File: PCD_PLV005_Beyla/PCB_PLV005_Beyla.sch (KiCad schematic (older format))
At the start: 5 parts, among them J1 PWR/QB, J2 Switch_In, U7 CRE1S2405SC

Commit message: Add Heartbeat_Buff signal pin
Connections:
- wire segments 31 -> 30
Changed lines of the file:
@@
 EESchema Schematic File Version 4
-EELAYER 30 0
+LIBS:PCB_PLV005_Beyla-cache
+EELAYER 29 0
 EELAYER END
 $Descr USLetter 11000 8500
@@
 F6 "HEARTBEAT_ADDRESS_4" O R 6000 4450 50
 F7 "HEARTBEAT" O R 6000 4600 50
+F8 "HEARTBEAT_BUFF" O R 6000 4700 50
 $EndSheet
 $Comp
@@
 $EndComp
 Wire Wire Line
-	4850 3000 4650 3000
-Connection ~ 4650 3000
-Wire Wire Line
 	4650 3000 4250 3000

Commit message: Beyla Schematic Changes
Addressed changes from review of initial schematic
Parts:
- removed D1: Red, symbol PCB_PLV005_Beyla-rescue:TemplateProject-rescue_LED-Device-TemplateProject-cache
- removed J1: PWR/QB, symbol Connector:Conn_01x08_Female
- removed J2: Switch_In, symbol Connector:Conn_01x04_Female
- removed R18: 1k, symbol TemplateProject-rescue:R_US-Device
- removed U7: CRE1S2405SC, Converter_DCDC:Converter_DCDC_muRata_CRE1xxxxxxSC_THT, symbol Regulator_Switching:CRE1S2405SC
- added C8: 1uF, symbol Device:C
- added C9: 10uF, symbol Device:C
- added D1: RED, symbol Device:LED
- added J1: PWR/QB, symbol Connector_Generic:Conn_01x08
- added J2: Switch_In, symbol Connector_Generic:Conn_01x04
- added R18: 1k, symbol Device:R_US
- added R19: 0, symbol Device:R_US
- added VR1: Recom_R-78c-1.0, symbol boringlib:Recom_R-78c-1.0
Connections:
- net labels added: +5V
- wire segments 30 -> 41
- no-connect marks 0 -> 1
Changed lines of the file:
@@
 EESchema Schematic File Version 4
-LIBS:PCB_PLV005_Beyla-cache
-EELAYER 29 0
+EELAYER 30 0
 EELAYER END
 $Descr USLetter 11000 8500
@@
 	1    0    0    -1
 $EndComp
-$Comp
-L Connector:Conn_01x08_Female J1
-U 1 1 5FB80BE7
+Wire Wire Line
+	7100 3950 6900 3950
+Wire Wire Line
+	6900 3350 7100 3350
+Wire Wire Line
+	7100 3350 7100 3450
+Wire Wire Line
+	6250 4600 6000 4600
+Wire Wire Line
+	6250 4550 7100 4550
+Wire Wire Line
+	6000 4450 7100 4450
+Wire Wire Line
+	6000 4350 7100 4350
+Wire Wire Line
+	6000 4250 7100 4250
+Wire Wire Line
+	6000 4150 7100 4150
+Wire Wire Line
+	6250 4550 6250 4600
+Wire Wire Line
+	4100 4150 2800 4150
+Wire Wire Line
+	2650 4250 2800 4250
+Wire Wire Line
+	2800 4250 2800 4150
+Connection ~ 2800 4150
+Wire Wire Line
+	2800 4150 2650 4150
+Wire Wire Line
+	2650 4450 2800 4450
+$Comp
+L power:GND #PWR0102
+U 1 1 5FB9ACDA
+P 2800 5100
+F 0 "#PWR0102" H 2800 4850 50  0001 C CNN
+F 1 "GND" H 2805 4927 50  0000 C CNN
+F 2 "" H 2800 5100 50  0001 C CNN
+F 3 "" H 2800 5100 50  0001 C CNN
+	1    2800 5100
+	1    0    0    -1
+$EndComp
+Wire Wire Line
+	6900 3350 6900 3600
+Wire Wire Line
+	7100 4050 6250 4050
+Wire Wire Line
+	6250 4050 6250 3000
+Wire Wire Line
+	6250 3000 5800 3000
+$Comp
+L Device:C C8
+U 1 1 5FBF38DA
+P 5800 3300
+F 0 "C8" H 5915 3346 50  0000 L CNN
+F 1 "1uF" H 5915 3255 50  0000 L CNN
+F 2 "" H 5838 3150 50  0001 C CNN
+F 3 "~" H 5800 3300 50  0001 C CNN
+	1    5800 3300
+	1    0    0    -1
+$EndComp
+$Comp
+L Device:C C9
+U 1 1 5FBF4C36
+P 4550 3300
+F 0 "C9" H 4665 3346 50  0000 L CNN
+F 1 "10uF" H 4665 3255 50  0000 L CNN
+F 2 "" H 4588 3150 50  0001 C CNN
+F 3 "~" H 4550 3300 50  0001 C CNN
+	1    4550 3300
+	1    0    0    -1
+$EndComp
+Wire Wire Line
+	6900 3600 5800 3600
+Connection ~ 6900 3600
+Wire Wire Line
+	6900 3600 6900 3950
+Wire Wire Line
+	5200 3600 5200 3350
+Wire Wire Line
+	5800 3450 5800 3600
+Connection ~ 5800 3600
+Wire Wire Line
+	5800 3600 5200 3600
+Wire Wire Line
+	5800 3150 5800 3000
+Connection ~ 5800 3000
+Wire Wire Line
+	5800 3000 5600 3000
+Wire Wire Line
+	4800 3000 4550 3000
+Wire Wire Line
+	4550 3000 4550 3150
+Wire Wire Line
+	4550 3450 4550 3600
+Wire Wire Line
+	4550 3600 5200 3600
+Connection ~ 5200 3600
+$Comp
+L power:+5V #PWR0103
+U 1 1 5FBFDEDC
+P 4550 2950
+F 0 "#PWR0103" H 4550 2800 50  0001 C CNN
+F 1 "+5V" H 4565 3123 50  0000 C CNN
+F 2 "" H 4550 2950 50  0001 C CNN
+F 3 "" H 4550 2950 50  0001 C CNN
+	1    4550 2950
+	1    0    0    -1
+$EndComp
+Connection ~ 4550 3000
+$Comp
+L Device:LED D1
+U 1 1 5FBFEF04
+P 4050 3000
+F 0 "D1" H 4043 3217 50  0000 C CNN
+F 1 "RED" H 4043 3126 50  0000 C CNN
+F 2 "" H 4050 3000 50  0001 C CNN
+F 3 "~" H 4050 3000 50  0001 C CNN
+	1    4050 3000
+	1    0    0    -1
+$EndComp
+$Comp
+L Device:R_US R18
+U 1 1 5FC06267
+P 3550 3300
+F 0 "R18" H 3618 3346 50  0000 L CNN
+F 1 "1k" H 3618 3255 50  0000 L CNN
+F 2 "" V 3590 3290 50  0001 C CNN
+F 3 "~" H 3550 3300 50  0001 C CNN
+	1    3550 3300
+	1    0    0    -1
+$EndComp
+Wire Wire Line
+	3900 3000 3550 3000
+Wire Wire Line
+	3550 3000 3550 3150
+Wire Wire Line
+	3550 3450 3550 3600
+Wire Wire Line
+	3550 3600 4550 3600
+Connection ~ 4550 3600
+Wire Wire Line
+	4200 3000 4550 3000
+$Comp
+L boringlib:Recom_R-78c-1.0 VR1
+U 1 1 5FC17AF0
+P 5200 3000
+F 0 "VR1" H 5200 3315 50  0000 C CNN
+F 1 "Recom_R-78c-1.0" H 5200 3224 50  0000 C CNN
+F 2 "" H 5400 2700 50  0001 C CNN
+F 3 "https://d311uvhi8lkjbj.cloudfront.net/media/Datasheet/pdf/.f91HWzyW/.t321978fcd1ad139cbfa2/Datasheet-260/R-78C-1_0.pdf" H 5400 2700 50  0001 C CNN
+	1    5200 3000
+	-1   0    0    -1
+$EndComp
+NoConn ~ 7100 4650
+Wire Wire Line
+	4550 2950 4550 3000
+$Comp
+L Connector_Generic:Conn_01x08 J1
+U 1 1 5FC2996A
 P 7300 4250
-F 0 "J1" H 7328 4226 50  0000 L CNN
-F 1 "PWR/QB" H 7328 4135 50  0000 L CNN
+F 0 "J1" H 7380 4242 50  0000 L CNN
+F 1 "PWR/QB" H 7380 4151 50  0000 L CNN
 F 2 "" H 7300 4250 50  0001 C CNN
 F 3 "~" H 7300 4250 50  0001 C CNN
@@
 	1    0    0    -1
 $EndComp
-Wire Wire Line
-	7100 3950 6900 3950
-Wire Wire Line
-	6900 3950 6900 3400
-Wire Wire Line
-	6900 3350 7100 3350
-Wire Wire Line
-	7100 3350 7100 3450
-Wire Wire Line
-	6250 4600 6000 4600
-Wire Wire Line
-	6250 4550 7100 4550
-Wire Wire Line
-	6000 4450 7100 4450
-Wire Wire Line
-	6000 4350 7100 4350
-Wire Wire Line
-	6000 4250 7100 4250
-Wire Wire Line
-	6000 4150 7100 4150
-Wire Wire Line
-	6250 4550 6250 4600
-$Comp
-L Connector:Conn_01x04_Female J2
-U 1 1 5FB96598
+$Comp
+L Connector_Generic:Conn_01x04 J2
+U 1 1 5FC2E912
 P 2450 4350
-F 0 "J2" H 2342 3925 50  0000 C CNN
-F 1 "Switch_In" H 2342 4016 50  0000 C CNN
+F 0 "J2" H 2368 3925 50  0000 C CNN
+F 1 "Switch_In" H 2368 4016 50  0000 C CNN
 F 2 "" H 2450 4350 50  0001 C CNN
 F 3 "~" H 2450 4350 50  0001 C CNN
@@
 	-1   0    0    1
 $EndComp
-Wire Wire Line
-	4100 4150 2800 4150
-Wire Wire Line
-	2650 4250 2800 4250
-Wire Wire Line
-	2800 4250 2800 4150
-Connection ~ 2800 4150
-Wire Wire Line
-	2800 4150 2650 4150
-Wire Wire Line
-	2650 4450 2800 4450
-Wire Wire Line
-	2800 4350 2650 4350
+$Comp
+L Device:R_US R19
+U 1 1 5FC33E92
+P 2800 4850
+F 0 "R19" H 2868 4896 50  0000 L CNN
+F 1 "0" H 2868 4805 50  0000 L CNN
+F 2 "" V 2840 4840 50  0001 C CNN
+F 3 "~" H 2800 4850 50  0001 C CNN
+	1    2800 4850
+	1    0    0    -1
+$EndComp
+Wire Wire Line
+	2800 4450 2800 4700
+Wire Wire Line
+	2800 5100 2800 5000
+$Comp
+L power:+5V #PWR0104
+U 1 1 5FC3DBBE
+P 2900 4350
+F 0 "#PWR0104" H 2900 4200 50  0001 C CNN
+F 1 "+5V" H 2915 4523 50  0000 C CNN
+F 2 "" H 2900 4350 50  0001 C CNN
+F 3 "" H 2900 4350 50  0001 C CNN
+	1    2900 4350
+	1    0    0    -1
+$EndComp
+Wire Wire Line
+	2650 4350 2800 4350
 Wire Wire Line
 	2800 4350 2800 4450
 Connection ~ 2800 4450
 Wire Wire Line
-	2800 4450 2800 4600
-$Comp
-L power:GND #PWR0102
-U 1 1 5FB9ACDA
-P 2800 4600
-F 0 "#PWR0102" H 2800 4350 50  0001 C CNN
-F 1 "GND" H 2805 4427 50  0000 C CNN
-F 2 "" H 2800 4600 50  0001 C CNN
-F 3 "" H 2800 4600 50  0001 C CNN
-	1    2800 4600
-	1    0    0    -1
-$EndComp
-$Comp
-L Regulator_Switching:CRE1S2405SC U7
-U 1 1 5FB97432
-P 5150 3200
-F 0 "U7" H 5150 3667 50  0000 C CNN
-F 1 "CRE1S2405SC" H 5150 3576 50  0000 C CNN
-F 2 "Converter_DCDC:Converter_DCDC_muRata_CRE1xxxxxxSC_THT" H 5150 2800 50  0001 C CNN
-F 3 "http://power.murata.com/datasheet?/data/power/ncl/kdc_cre1.pdf" H 5150 2700 50  0001 C CNN
-	1    5150 3200
-	-1   0    0    -1
-$EndComp
-Wire Wire Line
-	6300 3000 5650 3000
-$Comp
-L PCB_PLV005_Beyla-rescue:TemplateProject-rescue_LED-Device-TemplateProject-cache D1
-U 1 1 5FBAAA01
-P 4100 3000
-F 0 "D1" H 4093 3216 50  0000 C CNN
-F 1 "Red" H 4093 3125 50  0000 C CNN
-F 2 "" H 4100 3000 50  0001 C CNN
-F 3 "" H 4100 3000 50  0001 C CNN
-	1    4100 3000
-	1    0    0    -1
-$EndComp
-$Comp
-L TemplateProject-rescue:R_US-Device R18
-U 1 1 5FBACDDB
-P 3650 3000
-F 0 "R18" V 3855 3000 50  0000 C CNN
-F 1 "1k" V 3764 3000 50  0000 C CNN
-F 2 "" V 3690 2990 50  0001 C CNN
-F 3 "" H 3650 3000 50  0001 C CNN
-	1    3650 3000
-	0    -1   -1   0
-$EndComp
-$Comp
-L power:GND #PWR0103
-U 1 1 5FBB007E
-P 3350 3000
-F 0 "#PWR0103" H 3350 2750 50  0001 C CNN
-F 1 "GND" H 3355 2827 50  0000 C CNN
-F 2 "" H 3350 3000 50  0001 C CNN
-F 3 "" H 3350 3000 50  0001 C CNN
-	1    3350 3000
-	0    1    1    0
-$EndComp
-Wire Wire Line
-	4650 3000 4250 3000
-Wire Wire Line
-	3950 3000 3800 3000
-Wire Wire Line
-	4650 3400 3400 3400
-Wire Wire Line
-	3350 3000 3400 3000
-Wire Wire Line
-	5650 3400 6900 3400
-Connection ~ 6900 3400
-Wire Wire Line
-	6900 3400 6900 3350
-Wire Wire Line
-	7100 4050 6300 4050
-Wire Wire Line
-	6300 4050 6300 3000
-Wire Wire Line
-	3400 3400 3400 3000
-Connection ~ 3400 3000
-Wire Wire Line
-	3400 3000 3500 3000
+	2900 4350 2800 4350
+Connection ~ 2800 4350
 $EndSCHEMATC

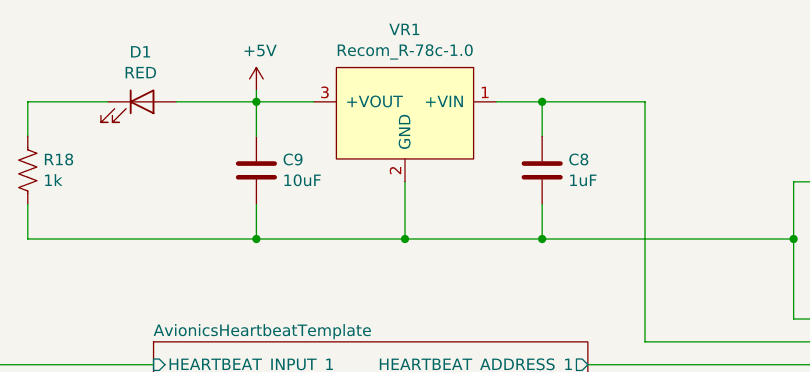
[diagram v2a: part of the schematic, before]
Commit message: Fix regulator issue.
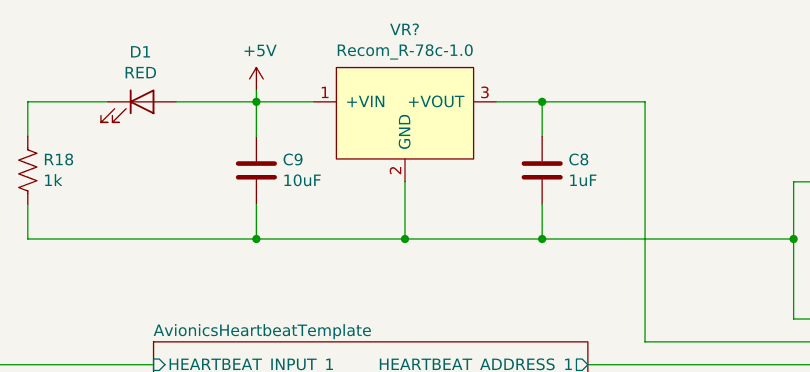
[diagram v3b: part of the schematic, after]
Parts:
- removed VR1: Recom_R-78c-1.0, symbol boringlib:Recom_R-78c-1.0
- added VR?: Recom_R-78c-1.0, BoringFootprints:Recom_R-78c-1.0, symbol boringlib:Recom_R-78c-1.0
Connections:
- net +5V: now also VR?.1 (+VIN)
- net GND: now also VR?.2 (GND)
- net at C8.1, J1.2 (Pin_2): now also VR?.3 (+VOUT)
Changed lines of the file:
@@
 EESchema Schematic File Version 4
-EELAYER 30 0
+LIBS:PCB_PLV005_Beyla-cache
+EELAYER 29 0
 EELAYER END
 $Descr USLetter 11000 8500
@@
 Wire Wire Line
 	4200 3000 4550 3000
-$Comp
-L boringlib:Recom_R-78c-1.0 VR1
-U 1 1 5FC17AF0
-P 5200 3000
-F 0 "VR1" H 5200 3315 50  0000 C CNN
-F 1 "Recom_R-78c-1.0" H 5200 3224 50  0000 C CNN
-F 2 "" H 5400 2700 50  0001 C CNN
-F 3 "https://d311uvhi8lkjbj.cloudfront.net/media/Datasheet/pdf/.f91HWzyW/.t321978fcd1ad139cbfa2/Datasheet-260/R-78C-1_0.pdf" H 5400 2700 50  0001 C CNN
-	1    5200 3000
-	-1   0    0    -1
-$EndComp
 NoConn ~ 7100 4650
 Wire Wire Line
@@
 	2900 4350 2800 4350
 Connection ~ 2800 4350
+$Comp
+L boringlib:Recom_R-78c-1.0 VR?
+U 1 1 5FC3D4E7
+P 5200 3000
+F 0 "VR?" H 5200 3315 50  0000 C CNN
+F 1 "Recom_R-78c-1.0" H 5200 3224 50  0000 C CNN
+F 2 "BoringFootprints:Recom_R-78c-1.0" H 5400 2700 50  0001 C CNN
+F 3 "" H 5400 2700 50  0001 C CNN
+	1    5200 3000
+	1    0    0    -1
+$EndComp
 $EndSCHEMATC
